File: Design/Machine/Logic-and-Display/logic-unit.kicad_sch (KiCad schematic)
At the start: 0 parts

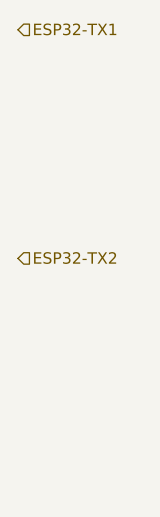
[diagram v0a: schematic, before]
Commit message: feat: schematics w/out buzzer, some LEDS, matrix
add schematics for LEDs and time display, missing FC-16 module (8x32 matrix) connection, left priority, right side LEDS, and buzzer
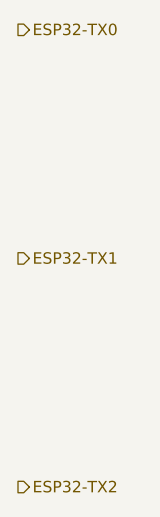
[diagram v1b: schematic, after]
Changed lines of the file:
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@@
 (kicad_sch (version 20230121) (generator eeschema)
   (paper "A4")
-  (hierarchical_label "ESP32-TX2" (shape input) (at 152.4 101.6 0) (fields_autoplaced)
+  (hierarchical_label "ESP32-TX0" (shape output) (at 152.4 76.2 0) (fields_autoplaced)
     (effects (font (size 1.27 1.27)) (justify left))
   )
-  (hierarchical_label "ESP32-TX1" (shape input) (at 152.4 76.2 0) (fields_autoplaced)
+  (hierarchical_label "ESP32-TX2" (shape output) (at 152.4 127 0) (fields_autoplaced)
     (effects (font (size 1.27 1.27)) (justify left))
   )
+  (hierarchical_label "ESP32-TX1" (shape output) (at 152.4 101.6 0) (fields_autoplaced)
+    (effects (font (size 1.27 1.27)) (justify left))
+  )

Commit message: feat: display units schematics
complete all display units schematics, this is left and right scores units; and LEDs, timer, and period display unit
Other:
- title: (none) -> Logic unit schematic
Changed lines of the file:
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@@
 (kicad_sch (version 20230121) (generator eeschema)
   (paper "A4")
+  (title_block
+    (title "Logic unit schematic")
+    (date "2023-05-19")
+    (rev "0.1.0")
+    (comment 1 "Schematic pending")
+  )
   (hierarchical_label "ESP32-TX0" (shape output) (at 152.4 76.2 0) (fields_autoplaced)
     (effects (font (size 1.27 1.27)) (justify left))

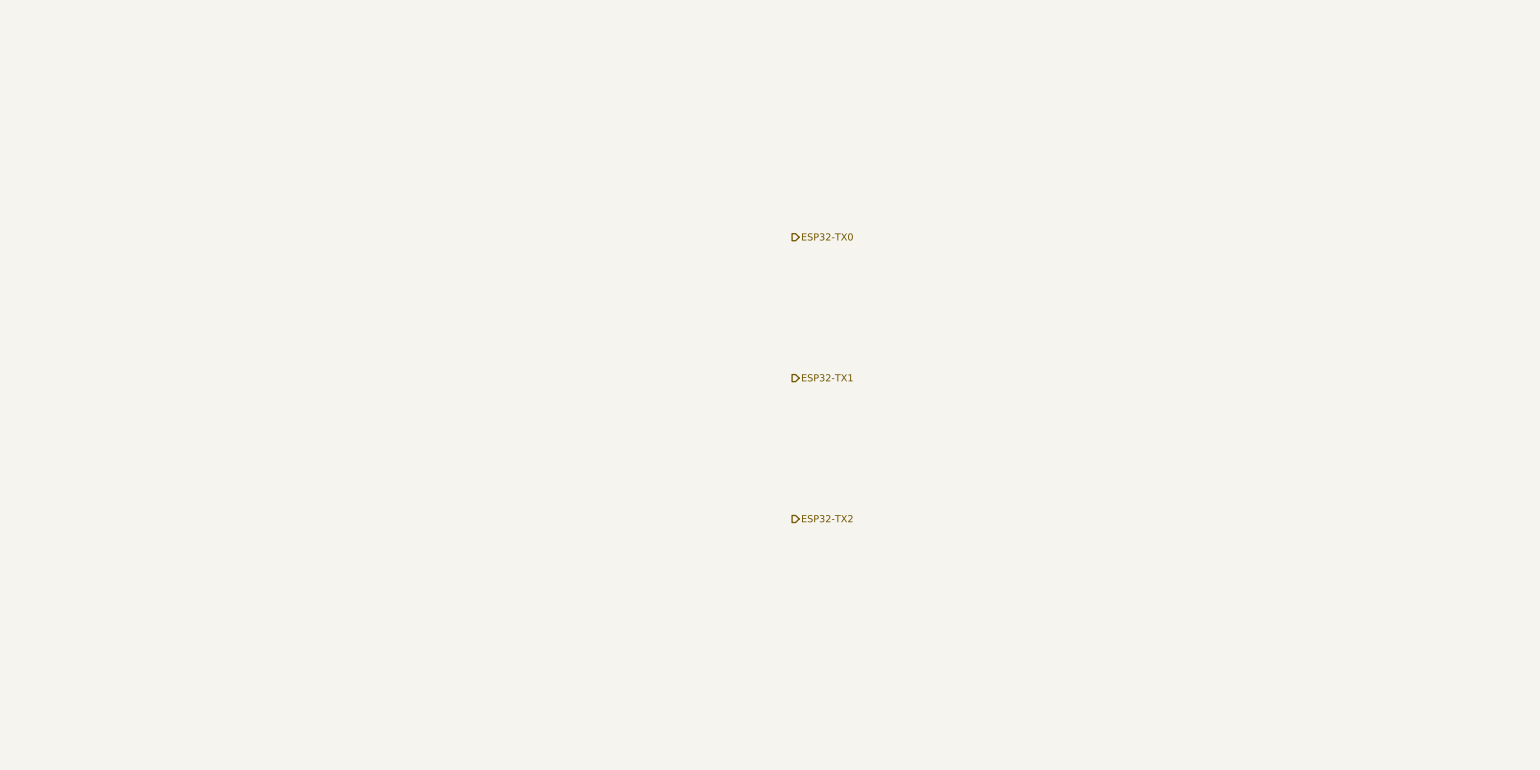
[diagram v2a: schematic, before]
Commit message: feat: logic unit schematics
make schematics for logic unit, power redundancy unit still missing
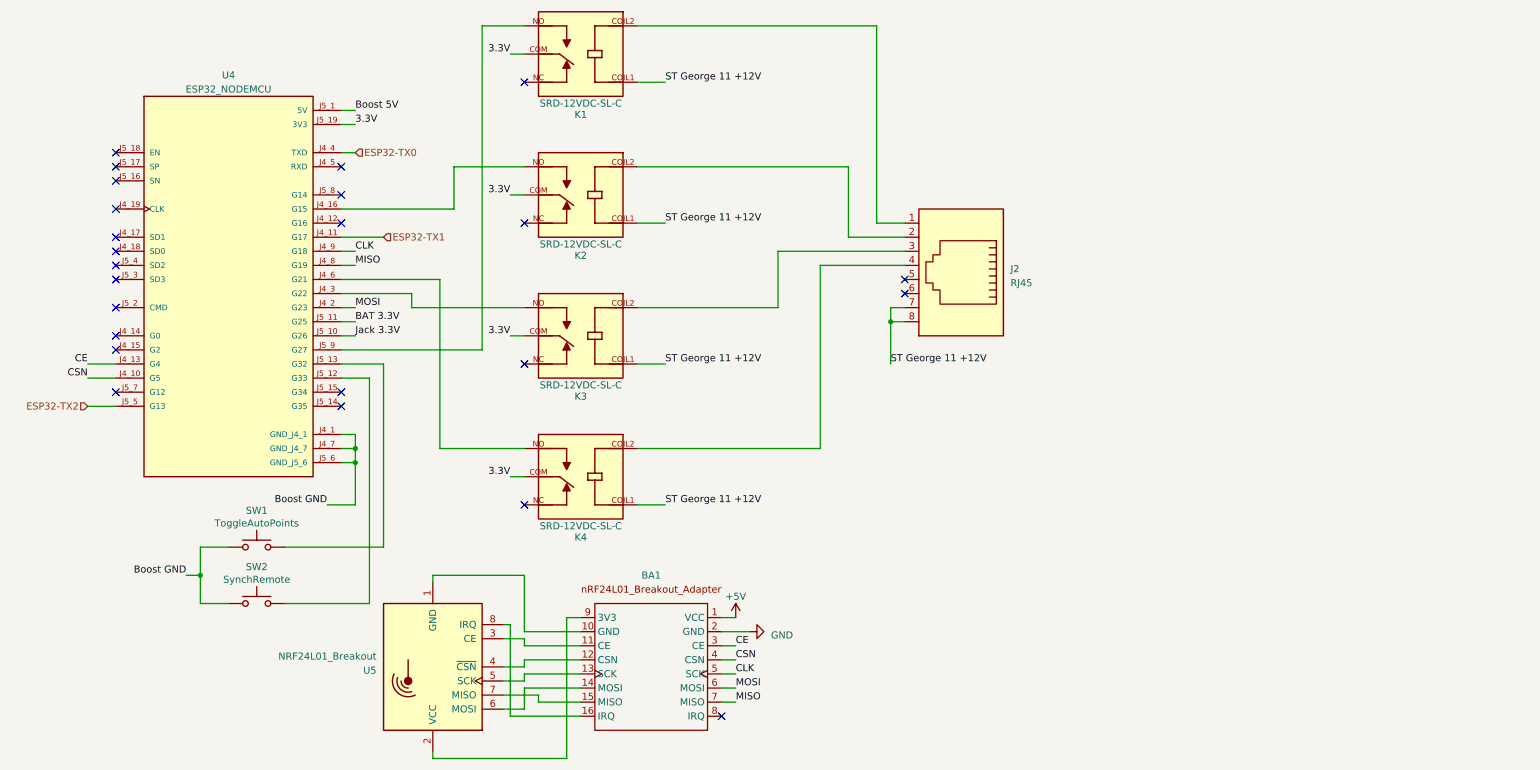
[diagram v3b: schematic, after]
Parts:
- added BA1: ~, Connector_PinSocket_2.54mm:PinSocket_1x08_P2.54mm_Vertical, symbol Arduino modules:nRF24L01_Breakout_Adapter_with_Voltage_Regulator
- added J2: RJ45, Connector_PinSocket_2.54mm:PinSocket_1x08_P2.54mm_Vertical, symbol Connector:RJ45
- added K1, K2, K3, K4: SRD-12VDC-SL-C, RELAY_SRD-12VDC-SL-C, symbol SRD-12VDC-SL-C:SRD-12VDC-SL-C
- added SW1: ToggleAutoPoints, Button_Switch_THT:SW_PUSH_6mm, symbol Switch:SW_Push
- added SW2: SynchRemote, Button_Switch_THT:SW_PUSH_6mm, symbol Switch:SW_Push
- added U4: ESP32_NODEMCU, ESP32_NODEMCU:MODULE_ESP32_NODEMCU, symbol ESP32_NODEMCU:ESP32_NODEMCU
- added U5: NRF24L01_Breakout, symbol RF:NRF24L01_Breakout
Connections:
- net ESP32-TX0: now also U4.J4_4 (TXD)
- net ESP32-TX1: now also U4.J4_11 (G17)
- net ESP32-TX2: now also U4.J5_5 (G13)
- new net: J2.1, K1.COIL2
- new net: K1.NO, U4.J5_9 (G27)
- new net: J2.4, K4.COIL2
- new net: K4.NO, U4.J4_6 (G21)
- new net: K2.NO, U4.J4_16 (G15)
- new net: K3.NO, U4.J4_3 (G22)
- new net: SW2.2, U4.J5_12 (G33)
- new net: SW1.2, U4.J5_13 (G32)
- new net: J2.2, K2.COIL2
- new net: J2.3, K3.COIL2
- new net: BA1.10 (GND), U5.1 (GND)
- new net: BA1.11 (CE), U5.3 (CE)
- new net: BA1.12 (CSN), U5.4 (~{CSN})
- new net: BA1.13 (SCK), U5.5 (SCK)
- new net: BA1.14 (MOSI), U5.6 (MOSI)
- new net: BA1.15 (MISO), U5.7 (MISO)
- new net: BA1.16 (IRQ), U5.8 (IRQ)
- new net: BA1.9 (3V3), U5.2 (VCC)
- new net +5V: BA1.1 (VCC)
- new net 3.3V: K1.COM, K2.COM, K3.COM, K4.COM, U4.J5_19 (3V3)
- new net BAT 3.3V: U4.J5_11 (G25)
- new net Boost 5V: U4.J5_1 (5V)
- new net Boost GND: SW1.1, SW2.1, U4.J4_1 (GND_J4_1), U4.J4_7 (GND_J4_7), U4.J5_6 (GND_J5_6)
- new net CE: BA1.3 (CE), U4.J4_13 (G4)
- new net CLK: BA1.5 (SCK), U4.J4_9 (G18)
- new net CSN: BA1.4 (CSN), U4.J4_10 (G5)
- new net GND: BA1.2 (GND)
- new net Jack 3.3V: U4.J5_10 (G26)
- new net MISO: BA1.7 (MISO), U4.J4_8 (G19)
- new net MOSI: BA1.6 (MOSI), U4.J4_2 (G23)
- new net ST George 11 +12V: J2.7, J2.8, K1.COIL1, K2.COIL1, K3.COIL1, K4.COIL1
- no-connect marks 0 -> 24

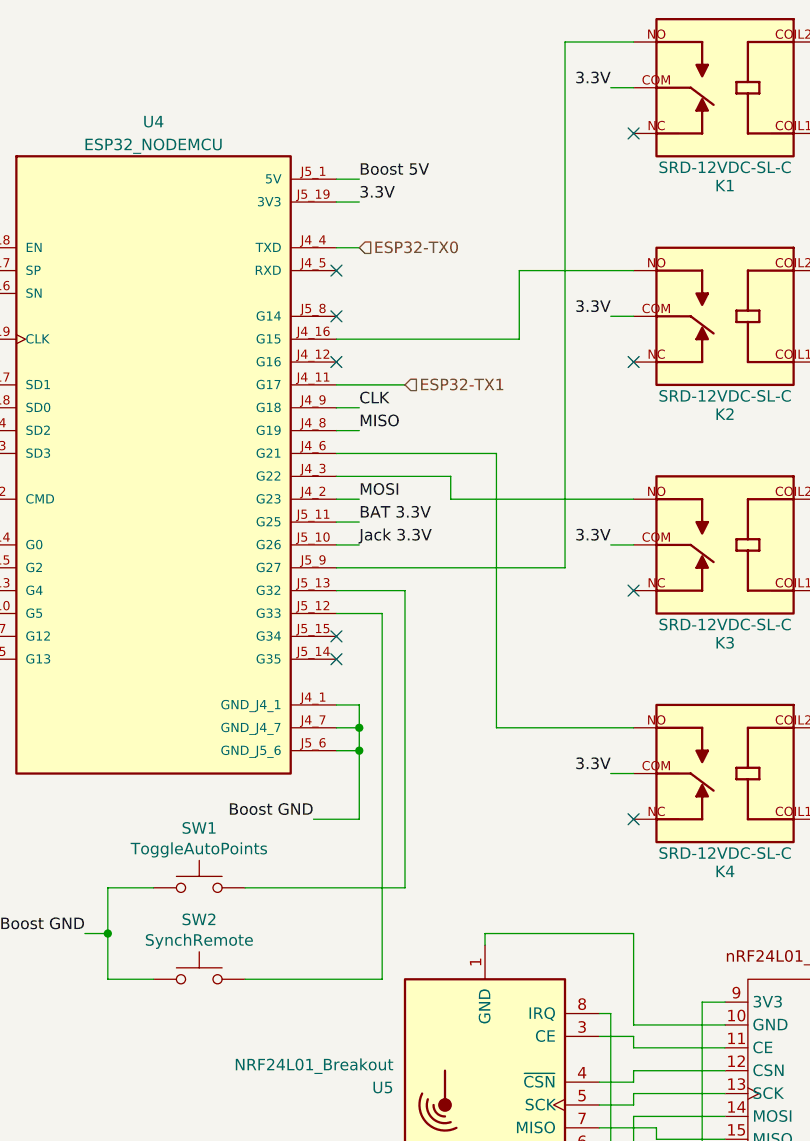
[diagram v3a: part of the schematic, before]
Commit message: fix: machine input pins
change machine input pins to use more appropriate ones
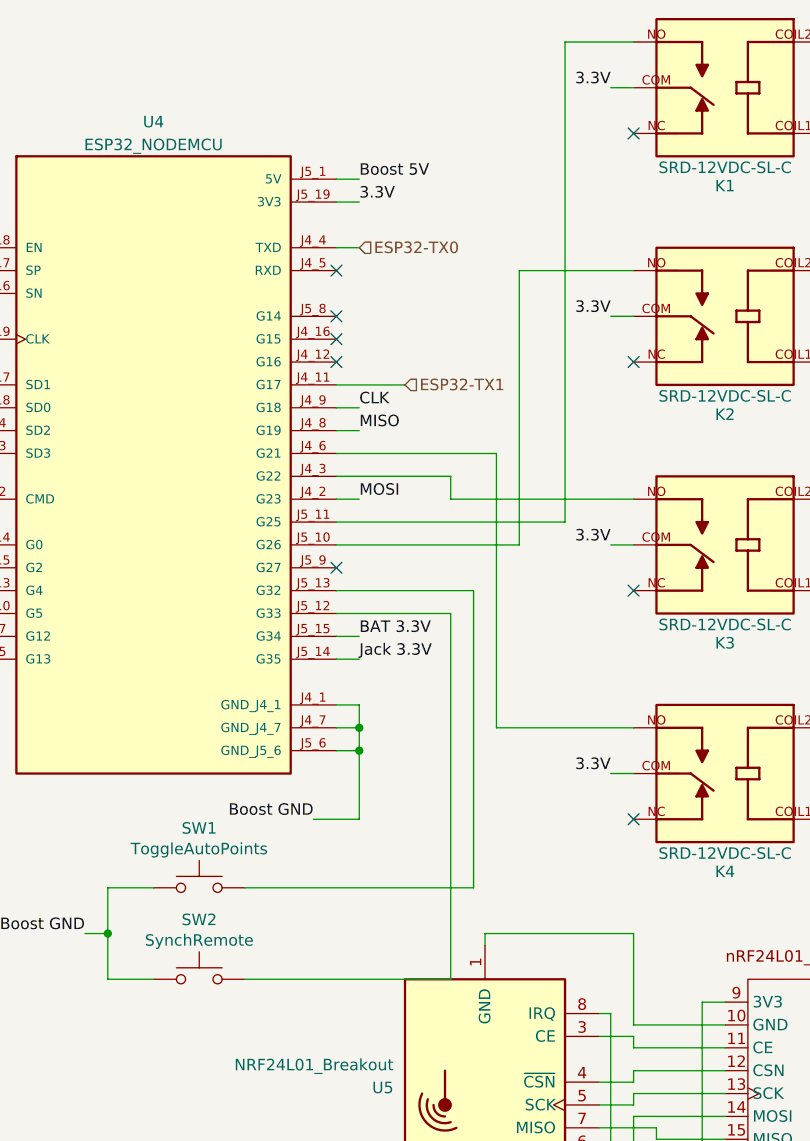
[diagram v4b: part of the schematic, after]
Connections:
- net BAT 3.3V: now also U4.J5_15 (G34); no longer U4.J5_11 (G25)
- net Jack 3.3V: now also U4.J5_14 (G35); no longer U4.J5_10 (G26)
- net at K1.NO: now also U4.J5_11 (G25); no longer U4.J5_9 (G27)
- net at U4.J4_16 (G15): no longer K2.NO
- new net: K2.NO, U4.J5_10 (G26)
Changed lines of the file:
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@@
   )
   (no_connect (at 30.48 76.2))
-  (no_connect (at 71.12 104.14))
+  (no_connect (at 71.12 96.52))
   (no_connect (at 30.48 63.5))
   (no_connect (at 104.14 99.06))
@@
   (no_connect (at 104.14 73.66))
   (no_connect (at 30.48 66.04))
-  (no_connect (at 71.12 106.68))
   (no_connect (at 30.48 78.74))
   (no_connect (at 30.48 60.96))
   (no_connect (at 30.48 83.82))
+  (no_connect (at 71.12 71.12))
   (no_connect (at 30.48 71.12))
   (no_connect (at 30.48 96.52))
@@
   (no_connect (at 71.12 63.5))
   (no_connect (at 30.48 104.14))
+  (wire (pts (xy 71.12 88.9) (xy 73.66 88.9))
+    (stroke (width 0) (type default))
+  )
   (wire (pts (xy 104.14 157.48) (xy 104.14 161.29))
     (stroke (width 0) (type default))
@@
     (stroke (width 0) (type default))
   )
-  (wire (pts (xy 91.44 71.12) (xy 71.12 71.12))
-    (stroke (width 0) (type default))
-  )
   (wire (pts (xy 101.6 43.18) (xy 104.14 43.18))
     (stroke (width 0) (type default))
   )
+  (wire (pts (xy 71.12 91.44) (xy 96.52 91.44))
+    (stroke (width 0) (type default))
+  )
   (wire (pts (xy 162.56 76.2) (xy 162.56 63.5))
     (stroke (width 0) (type default))
@@
     (stroke (width 0) (type default))
   )
+  (wire (pts (xy 91.44 93.98) (xy 71.12 93.98))
+    (stroke (width 0) (type default))
+  )
   (wire (pts (xy 162.56 63.5) (xy 124.46 63.5))
     (stroke (width 0) (type default))
@@
     (stroke (width 0) (type default))
   )
+  (wire (pts (xy 71.12 104.14) (xy 73.66 104.14))
+    (stroke (width 0) (type default))
+  )
   (wire (pts (xy 114.3 160.02) (xy 106.68 160.02))
     (stroke (width 0) (type default))
   )
-  (wire (pts (xy 91.44 71.12) (xy 91.44 63.5))
-    (stroke (width 0) (type default))
-  )
-  (wire (pts (xy 78.74 132.08) (xy 60.96 132.08))
+  (wire (pts (xy 86.36 132.08) (xy 60.96 132.08))
     (stroke (width 0) (type default))
   )
@@
     (stroke (width 0) (type default))
   )
-  (wire (pts (xy 71.12 101.6) (xy 76.2 101.6))
+  (wire (pts (xy 71.12 101.6) (xy 83.82 101.6))
     (stroke (width 0) (type default))
   )
@@
     (stroke (width 0) (type default))
   )
-  (wire (pts (xy 76.2 142.24) (xy 60.96 142.24))
+  (wire (pts (xy 83.82 142.24) (xy 60.96 142.24))
     (stroke (width 0) (type default))
   )
@@
     (stroke (width 0) (type default))
   )
-  (wire (pts (xy 96.52 96.52) (xy 71.12 96.52))
-    (stroke (width 0) (type default))
-  )
   (wire (pts (xy 83.82 86.36) (xy 83.82 88.9))
     (stroke (width 0) (type default))
@@
     (stroke (width 0) (type default))
   )
+  (wire (pts (xy 91.44 63.5) (xy 91.44 93.98))
+    (stroke (width 0) (type default))
+  )
   (wire (pts (xy 73.66 116.84) (xy 73.66 124.46))
     (stroke (width 0) (type default))
@@
     (stroke (width 0) (type default))
   )
-  (wire (pts (xy 71.12 88.9) (xy 73.66 88.9))
-    (stroke (width 0) (type default))
-  )
   (wire (pts (xy 71.12 53.34) (xy 73.66 53.34))
     (stroke (width 0) (type default))
   )
+  (wire (pts (xy 71.12 106.68) (xy 73.66 106.68))
+    (stroke (width 0) (type default))
+  )
   (wire (pts (xy 101.6 162.56) (xy 101.6 146.05))
     (stroke (width 0) (type default))
@@
     (stroke (width 0) (type default))
   )
-  (wire (pts (xy 96.52 38.1) (xy 96.52 96.52))
-    (stroke (width 0) (type default))
-  )
-  (wire (pts (xy 71.12 91.44) (xy 73.66 91.44))
-    (stroke (width 0) (type default))
-  )
-  (wire (pts (xy 71.12 93.98) (xy 73.66 93.98))
+  (wire (pts (xy 96.52 38.1) (xy 96.52 91.44))
     (stroke (width 0) (type default))
   )
@@
     (stroke (width 0) (type default))
   )
-  (wire (pts (xy 76.2 101.6) (xy 76.2 142.24))
+  (wire (pts (xy 83.82 101.6) (xy 83.82 142.24))
     (stroke (width 0) (type default))
   )
@@
     (stroke (width 0) (type default))
   )
-  (wire (pts (xy 78.74 99.06) (xy 78.74 132.08))
+  (wire (pts (xy 86.36 99.06) (xy 86.36 132.08))
     (stroke (width 0) (type default))
   )
@@
     (stroke (width 0) (type default))
   )
-  (wire (pts (xy 71.12 99.06) (xy 78.74 99.06))
+  (wire (pts (xy 71.12 99.06) (xy 86.36 99.06))
     (stroke (width 0) (type default))
   )
@@
     (effects (font (size 1.27 1.27)) (justify right bottom))
   )
-  (label "BAT 3.3V" (at 73.66 91.44 0) (fields_autoplaced)
+  (label "BAT 3.3V" (at 73.66 104.14 0) (fields_autoplaced)
     (effects (font (size 1.27 1.27)) (justify left bottom))
   )
@@
     (effects (font (size 1.27 1.27)) (justify left bottom))
   )
-  (label "Jack 3.3V" (at 73.66 93.98 0) (fields_autoplaced)
-    (effects (font (size 1.27 1.27)) (justify left bottom))
-  )
+  (label "Jack 3.3V" (at 73.66 106.68 0) (fields_autoplaced)
+    (effects (font (size 1.27 1.27)) (justify left bottom))
+  )
